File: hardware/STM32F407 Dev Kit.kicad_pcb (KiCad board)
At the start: 2 copper layers, 65.2 x 70 mm, 153 parts, among them J1 GMSB0531112YEU, J10 Conn_01x04, J11 TBC 2.54mm 10A, J12 IMP34DT05, J2 Conn_01x06, J3 RJMG1S8008101BR, J4 B2B-XH-A(LF)(SN), J5 Conn_01x04, J7 SJ-3524-SMT, J8 GMSB0531112YEU, J9 Conn_01x04, SW1 SW TACT-SPST, SW2 SW TACT-SPST, SW3 SW TACT-SPST, U1 STM32F103CBT6, U2 DP83826IRHBR, U3 DRV8701ERGET, U4 DMHT6016LFJ-13, U5 ADS122C04IPW, U6 CS43L22, U7 STM32F407VGT6, U8 AP63203WU, U9 XC6206P182MR, Y1 ABM8G-8.000MHZ-18-D2Y-T, Y2 ABM8G-25.000MHZ-9-B4Y-T, Y3 ABM8G-8.000MHZ-18-D2Y-T

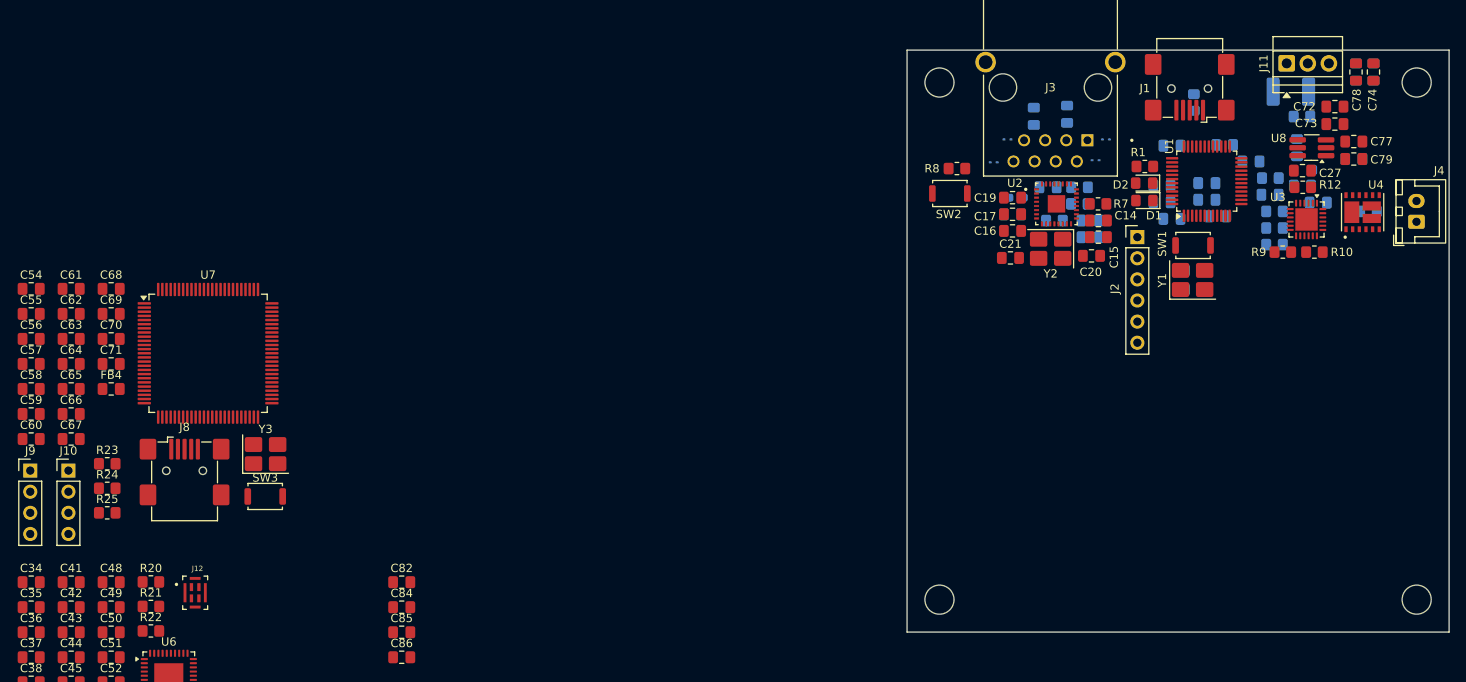
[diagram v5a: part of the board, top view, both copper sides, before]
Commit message: Place components for STM32F407
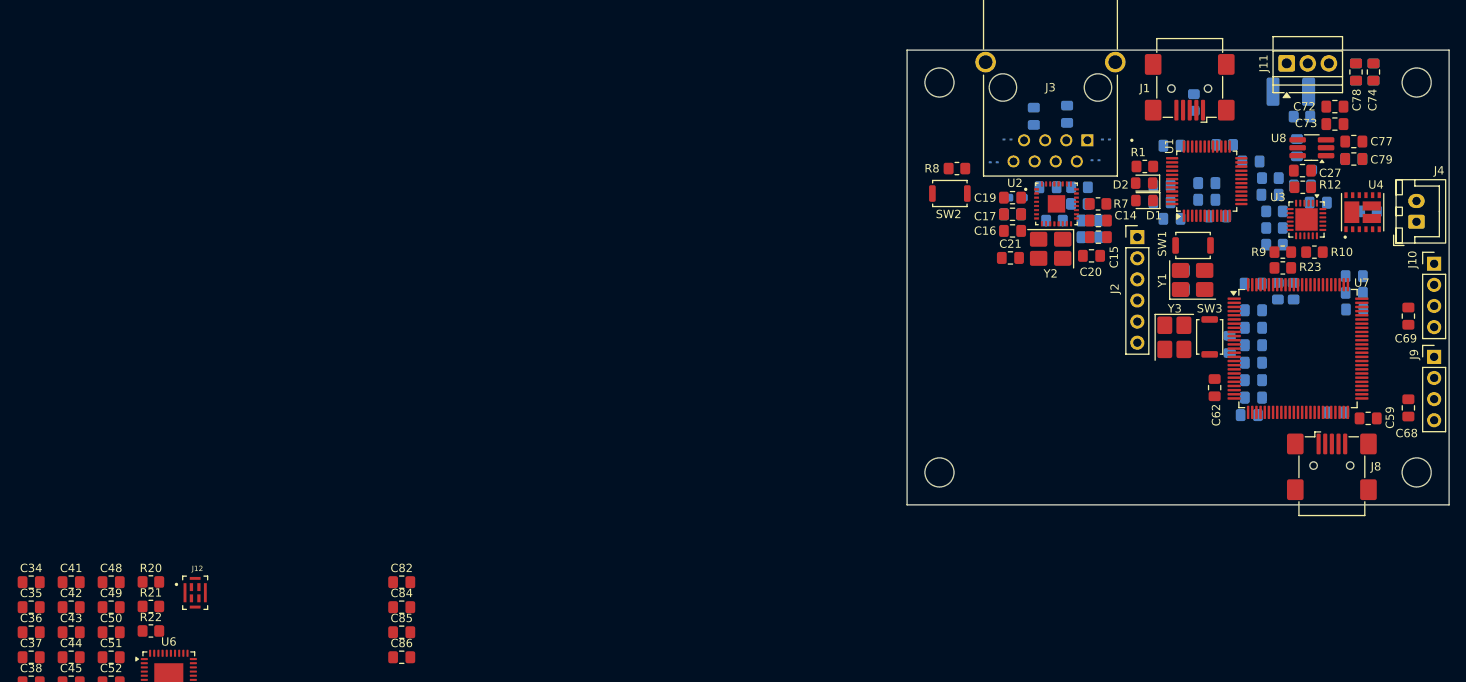
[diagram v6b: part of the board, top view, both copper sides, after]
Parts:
- C54, C55, C56, C57, C58, C60, C61, C63, C64, C65, C66, C67, C70, C71, FB4, R24, R25: moved to B.Cu
- moved J9 169.4 mm to (213.4, 86.9)
- moved J10 166.1 mm to (213.4, 75.7)
- moved C59 160.8 mm to (205.5, 94.3)
- moved C55 159.2 mm to (203.8, 79.2), turned to 180 degrees
- moved C54 159.2 mm to (203.8, 77.2), turned to 180 degrees
- moved C58 156.9 mm to (201.6, 93.6), turned to 180 degrees
- moved C68 156.7 mm to (210.3, 93.0), turned to -90 degrees
- moved C69 156.0 mm to (210.3, 82.0), turned to -90 degrees
- moved C61 154.4 mm to (203.8, 81.2), turned to 180 degrees
- moved C56 147.1 mm to (191.6, 78.1)
- moved C60 146.5 mm to (191.2, 93.9), turned to 180 degrees
- moved R24 144.7 mm to (196.5, 79.0), turned to 90 degrees
- moved C57 144.2 mm to (188.8, 85.4), turned to 90 degrees
- moved R23 143.3 mm to (195.2, 76.2)
- moved R25 143.3 mm to (194.6, 79.0), turned to -90 degrees
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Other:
- board size 65.2 x 70 mm -> 65.2 x 54.7 mm

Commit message: Place components for ADC
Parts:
- C28, C29, C31, C32, C33, FB2, R17: moved to B.Cu
- moved FB2 91.7 mm to (165.5, 84.3)
- moved C33 87.6 mm to (155.6, 80.1)
- moved U5 84.2 mm to (163.8, 83.5), turned to -90 degrees
- moved C32 83.8 mm to (157.7, 82.6)
- moved C31 79.1 mm to (157.7, 85.2)
- moved C29 78.2 mm to (162.5, 83.7), turned to 90 degrees
- moved C30 78.2 mm to (158.6, 83.8), turned to -90 degrees
- moved C28 75.8 mm to (165.5, 86.3)
- moved R17 73.5 mm to (164.8, 81.4), turned to 90 degrees
- moved J5 71.0 mm to (151.8, 80.1)
- moved R19 70.7 mm to (155.7, 85.2), turned to 180 degrees
- moved R18 70.4 mm to (155.7, 82.6), turned to 180 degrees
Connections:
- C30 pad 1: /[6] - ADC/AIN1 -> /[6] - ADC/AIN2
- C30 pad 2: /[6] - ADC/AIN2 -> /[6] - ADC/AIN1
- C31 pad 1: /[6] - ADC/AIN2 -> /[6] - ADC/AIN1
- C32 pad 1: /[6] - ADC/AIN1 -> /[6] - ADC/AIN2
- J5 pad 2: /[6] - ADC/SENSOR_PIN1 -> /[6] - ADC/SENSOR_PIN2
- J5 pad 3: /[6] - ADC/SENSOR_PIN2 -> /[6] - ADC/SENSOR_PIN1
- R18 pad 1: /[6] - ADC/AIN1 -> /[6] - ADC/AIN2
- R18 pad 2: /[6] - ADC/SENSOR_PIN1 -> /[6] - ADC/SENSOR_PIN2
- R19 pad 1: /[6] - ADC/AIN2 -> /[6] - ADC/AIN1
- R19 pad 2: /[6] - ADC/SENSOR_PIN2 -> /[6] - ADC/SENSOR_PIN1

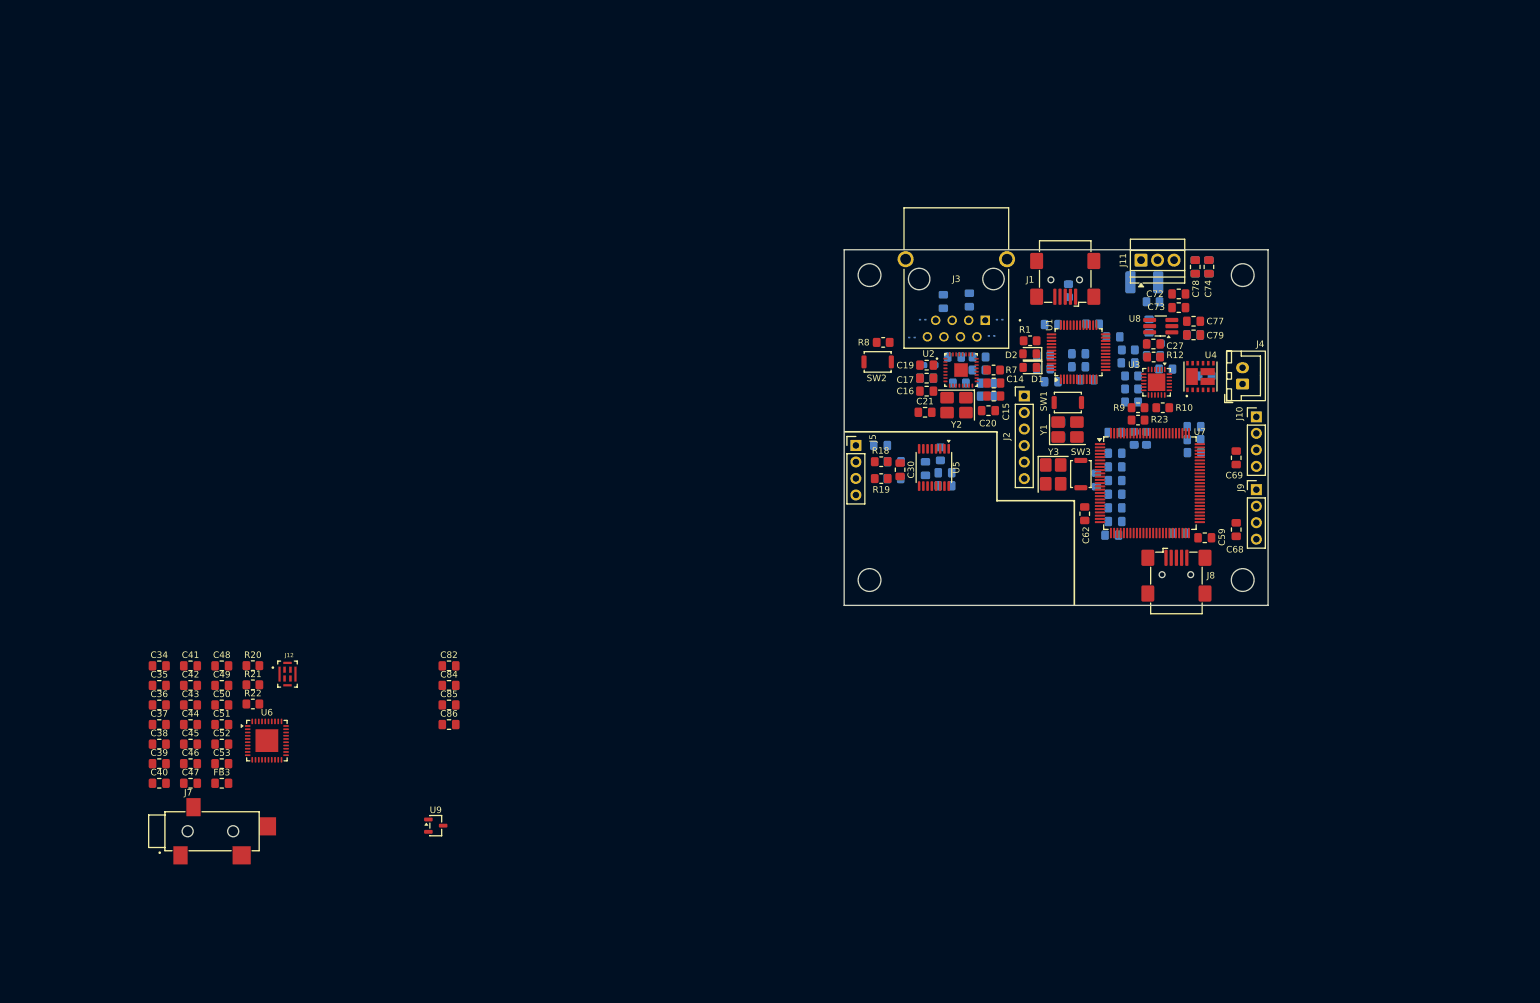
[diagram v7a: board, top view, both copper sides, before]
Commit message: Place components for DAC and Mic
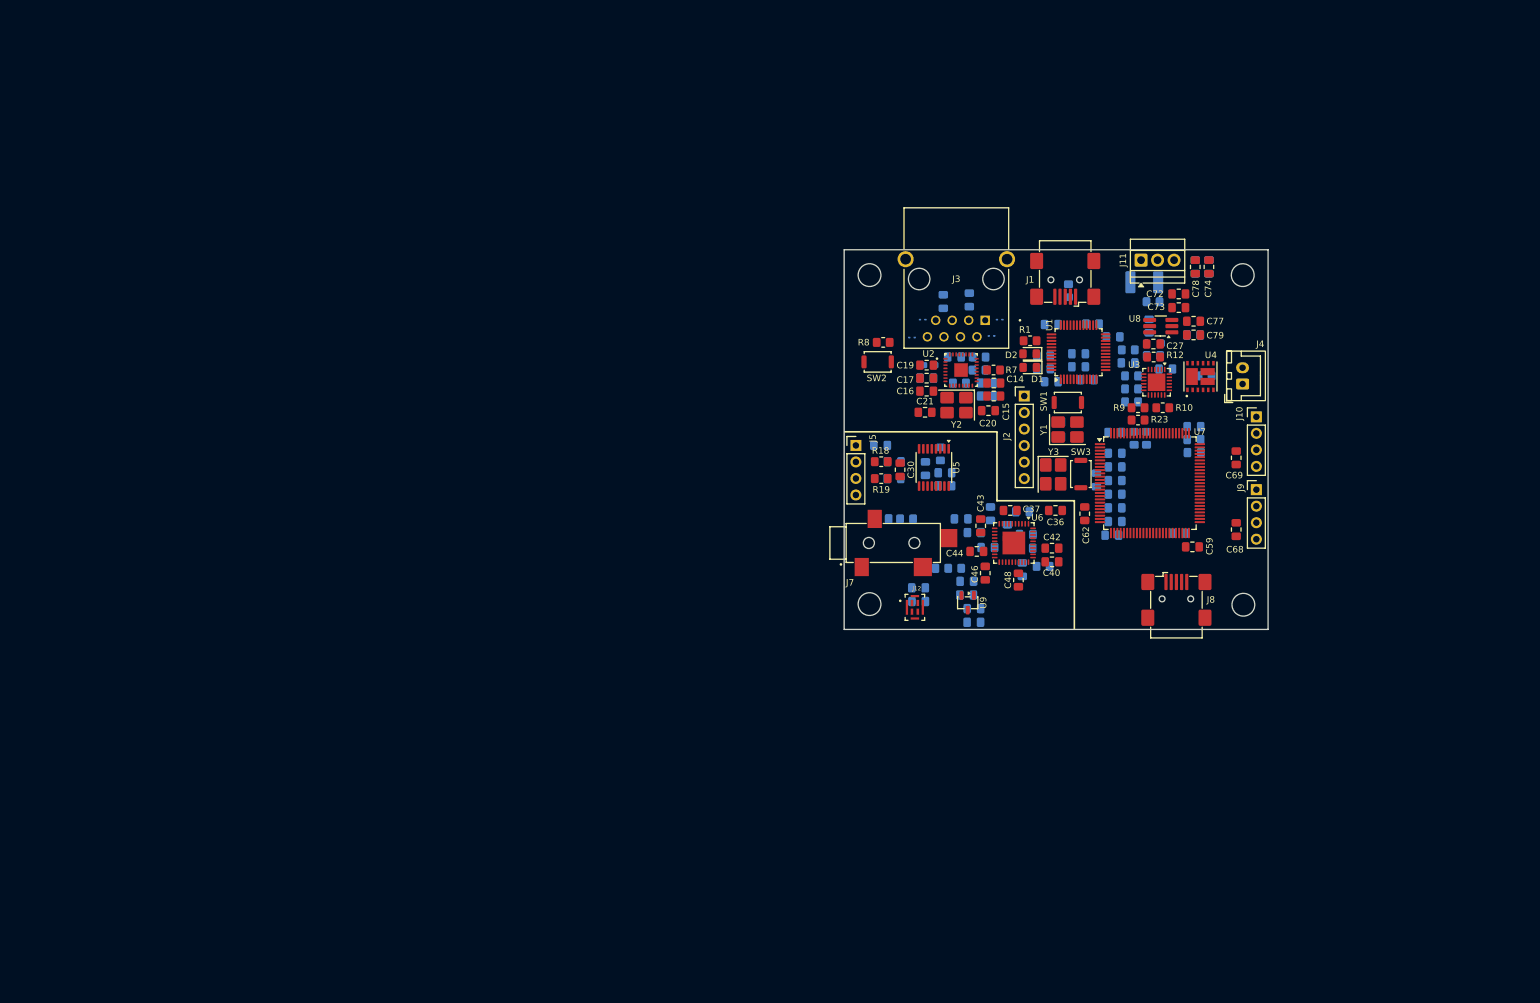
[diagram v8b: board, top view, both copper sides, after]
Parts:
- C34, C35, C38, C39, C41, C45, C47, C49, C50, C51, C52, C53, C82, C84, C85, C86, FB3, R20, R21, R22: moved to B.Cu
- moved C40 141.5 mm to (182.0, 98.0)
- moved C36 141.1 mm to (182.5, 90.1)
- moved C35 135.4 mm to (177.4, 90.3)
- moved C37 135.0 mm to (175.5, 90.1), turned to 180 degrees
- moved C42 134.2 mm to (182.0, 95.9)
- moved C39 133.5 mm to (172.5, 90.6), turned to 90 degrees
- moved C47 133.5 mm to (178.0, 95.9), turned to 180 degrees
- moved C45 132.5 mm to (178.0, 93.8), turned to 180 degrees
- moved C34 132.1 mm to (175.1, 93.3), turned to -90 degrees
- moved C38 129.5 mm to (170.0, 93.5)
- moved C46 125.7 mm to (171.7, 99.7), turned to -90 degrees
- moved C43 124.6 mm to (171.0, 92.5), turned to -90 degrees
- moved C49 124.4 mm to (177.4, 99.2), turned to -90 degrees
- moved C44 123.8 mm to (170.4, 96.4), turned to 180 degrees
- moved FB3 123.3 mm to (172.1, 95.8)
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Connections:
- C50 pad 1: Net-(J12-Pin_1) -> +3V3
- C52 pad 1: Net-(J12-Pin_1) -> +3V3
- J12 pad 1: Net-(J12-Pin_1) -> +3V3
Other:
- board size 65.2 x 54.7 mm -> 65.2 x 58.4 mm
